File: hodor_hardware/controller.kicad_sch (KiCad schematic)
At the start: 42 parts, among them J4 USB_C_Receptacle_USB2.0_16P, J8 Conn_01x04_Pin, J9 Conn_01x04_Pin, SW1 SW_RST, SW2 SW_BOOT, T21 SCL, T24 SDA, U1 ESP32-S3-WROOM-1_N8R2, U6 MAX811SEUS-T, U9 24LC256

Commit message: Schematic finished
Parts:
- removed C20: 100p, Capacitor_SMD:C_0402_1005Metric, symbol Device:C
- removed R29: 47R, Resistor_SMD:R_0402_1005Metric, symbol Device:R
- C14, C39: value 100n -> 100nF
- J8, J9: footprint (none) -> Connector_PinHeader_2.54mm:PinHeader_1x04_P2.54mm_Vertical
- T21, T24: now left out of the parts list
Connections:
- net ADC_IN5 is gone; now on an unnamed net: U1.17 (IO9)
- net ADC_CH1: now reaches R31.1
- net ADC_CH2: now reaches R30.1
- net ADC_CH3: now reaches R32.1
- net ADC_CH4: now reaches R36.1
- net at R1.1: now also U1.22 (IO14)
- net OUT_CTRL_1: now reaches U1.10 (IO17)
- net OUT_CTRL_2: now reaches U1.11 (IO18)
- net DRV_~{SF}: now reaches U1.16 (IO46)
- net DRV_PWM1: now reaches U1.24 (IO47)
- net DRV_PWM2: now reaches U1.25 (IO48)
- net DRV_EN: now reaches U1.26 (IO45)
- net ENCODER_A: now reaches U1.28 (IO35)
- net ENCODER_B: now reaches U1.29 (IO36)
- net INPUT_1: now reaches U1.30 (IO37)
- net INPUT_2: now reaches U1.31 (IO38)
- net INPUT_3: now reaches U1.32 (IO39)
- net INPUT_4: now reaches U1.33 (IO40)
- net SAFETY_~{CLR}: now reaches U1.34 (IO41)
- net SAFETY_TRIG: now reaches U1.35 (IO42)
- net RELAY_CTRL_1: now reaches U1.8 (IO15)
- net RELAY_CTRL_2: now reaches U1.9 (IO16)
- no-connect marks 4 -> 5
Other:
- note added: "Status LEDs"
- moved on the sheet: D1, D2, R1, R2

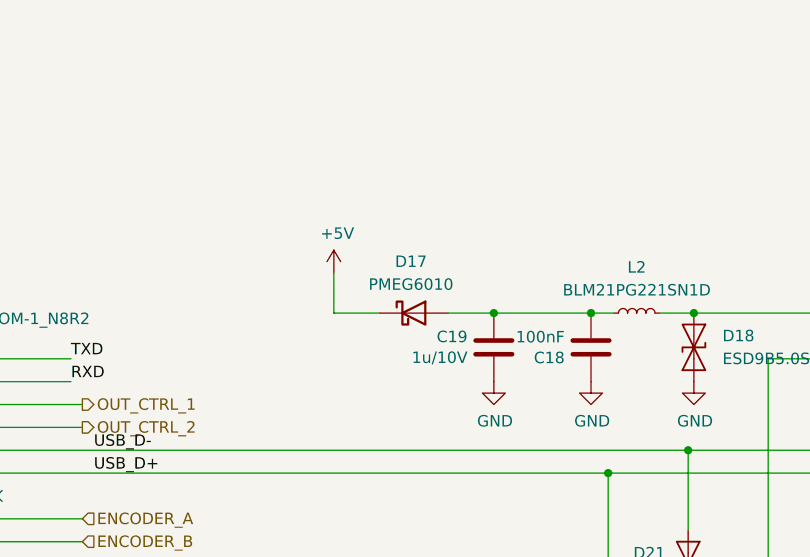
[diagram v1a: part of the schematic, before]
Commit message: Added USB switchover function for 5V
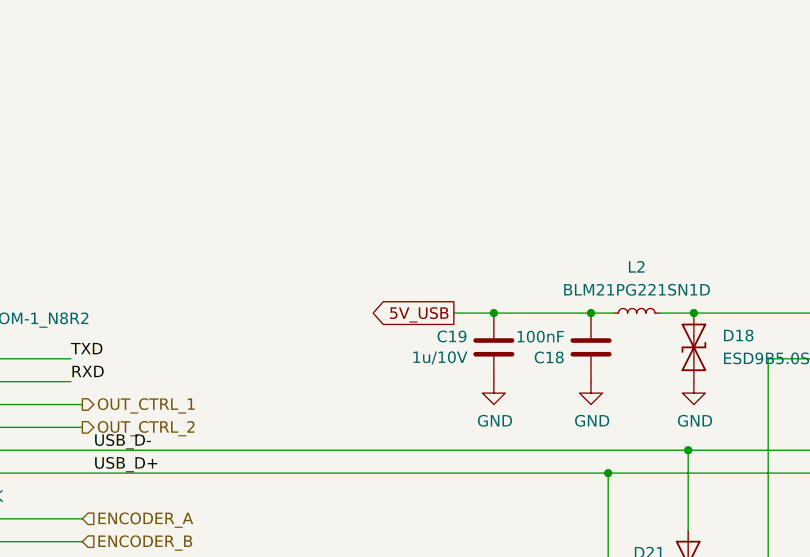
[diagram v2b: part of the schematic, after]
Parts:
- removed D17: PMEG6010, Diode_SMD:D_SOD-123F, symbol Device:D_Schottky
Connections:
- net 5V_USB: now reaches C18.1, C19.2, L2.1
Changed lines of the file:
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@@
 	(wire
 		(pts
-			(xy 171.45 45.72) (xy 166.37 45.72)
-		)
-		(stroke
-			(width 0)
-			(type default)
-		)
-	)
-	(wire
-		(pts
 			(xy 88.9 86.36) (xy 98.425 86.36)
 		)
@@
 		)
 	)
-	(wire
-		(pts
-			(xy 166.37 41.275) (xy 166.37 45.72)
-		)
-		(stroke
-			(width 0)
-			(type default)
-		)
-	)
 	(bus
 		(pts
@@
 	(wire
 		(pts
-			(xy 179.07 45.72) (xy 184.15 45.72)
+			(xy 179.705 45.72) (xy 184.15 45.72)
 		)
 		(stroke
@@
 		)
 	)
+	(global_label "5V_USB"
+		(shape output)
+		(at 179.705 45.72 180)
+		(fields_autoplaced yes)
+		(effects
+			(font
+				(size 1.27 1.27)
+			)
+			(justify right)
+		)
+		(property "Intersheetrefs" "${INTERSHEET_REFS}"
+			(at 169.6441 45.72 0)
+			(effects
+				(font
+					(size 1.27 1.27)
+				)
+				(justify right)
+			)
+		)
+	)
 	(hierarchical_label "RELAY_CTRL_1"
 		(shape output)
@@
 	)
 	(symbol
-		(lib_id "Device:D_Schottky")
-		(at 175.26 45.72 0)
-		(unit 1)
-		(exclude_from_sim no)
-		(in_bom yes)
-		(on_board yes)
-		(dnp no)
-		(fields_autoplaced yes)
-		(property "Reference" "D17"
-			(at 174.9425 40.005 0)
-			(effects
-				(font
-					(size 1.27 1.27)
-				)
-			)
-		)
-		(property "Value" "PMEG6010"
-			(at 174.9425 42.545 0)
-			(effects
-				(font
-					(size 1.27 1.27)
-				)
-			)
-		)
-		(property "Footprint" "Diode_SMD:D_SOD-123F"
-			(at 175.26 45.72 0)
-			(effects
-				(font
-					(size 1.27 1.27)
-				)
-				(hide yes)
-			)
-		)
-		(property "Datasheet" "~"
-			(at 175.26 45.72 0)
-			(effects
-				(font
-					(size 1.27 1.27)
-				)
-				(hide yes)
-			)
-		)
-		(property "Description" "Schottky diode"
-			(at 175.26 45.72 0)
-			(effects
-				(font
-					(size 1.27 1.27)
-				)
-				(hide yes)
-			)
-		)
-		(pin "2"
-		)
-		(pin "1"
-		)
-		(instances
-			(project "hodor_hardware"
-				(path "/2da01e60-41ef-423d-82f4-a5c8908d8b96/efd4ec69-52b7-4b82-b6f7-297e43729fd0"
-					(reference "D17")
-					(unit 1)
-				)
-			)
-		)
-	)
-	(symbol
 		(lib_id "Hodor-rescue:GND-power")
 		(at 46.355 130.81 0)
@@
 					(unit 1)
 				)
-			)
-		)
-	)
-	(symbol
-		(lib_id "Hodor-rescue:+5V-power")
-		(at 166.37 41.275 0)
-		(unit 1)
-		(exclude_from_sim no)
-		(in_bom yes)
-		(on_board yes)
-		(dnp no)
-		(property "Reference" "#PWR060"
-			(at 166.37 45.085 0)
-			(effects
-				(font
-					(size 1.27 1.27)
-				)
-				(hide yes)
-			)
-		)
-		(property "Value" "+5V"
-			(at 166.751 36.8808 0)
-			(effects
-				(font
-					(size 1.27 1.27)
-				)
-			)
-		)
-		(property "Footprint" ""
-			(at 166.37 41.275 0)
-			(effects
-				(font
-					(size 1.27 1.27)
-				)
-				(hide yes)
-			)
-		)
-		(property "Datasheet" ""
-			(at 166.37 41.275 0)
-			(effects
-				(font
-					(size 1.27 1.27)
-				)
-				(hide yes)
-			)
-		)
-		(property "Description" ""
-			(at 166.37 41.275 0)
-			(effects
-				(font
-					(size 1.27 1.27)
-				)
-				(hide yes)
-			)
-		)
-		(pin "1"
-		)
-		(instances
-			(project "hodor_hardware"
-				(path "/2da01e60-41ef-423d-82f4-a5c8908d8b96/efd4ec69-52b7-4b82-b6f7-297e43729fd0"
-					(reference "#PWR060")
-					(unit 1)
-				)

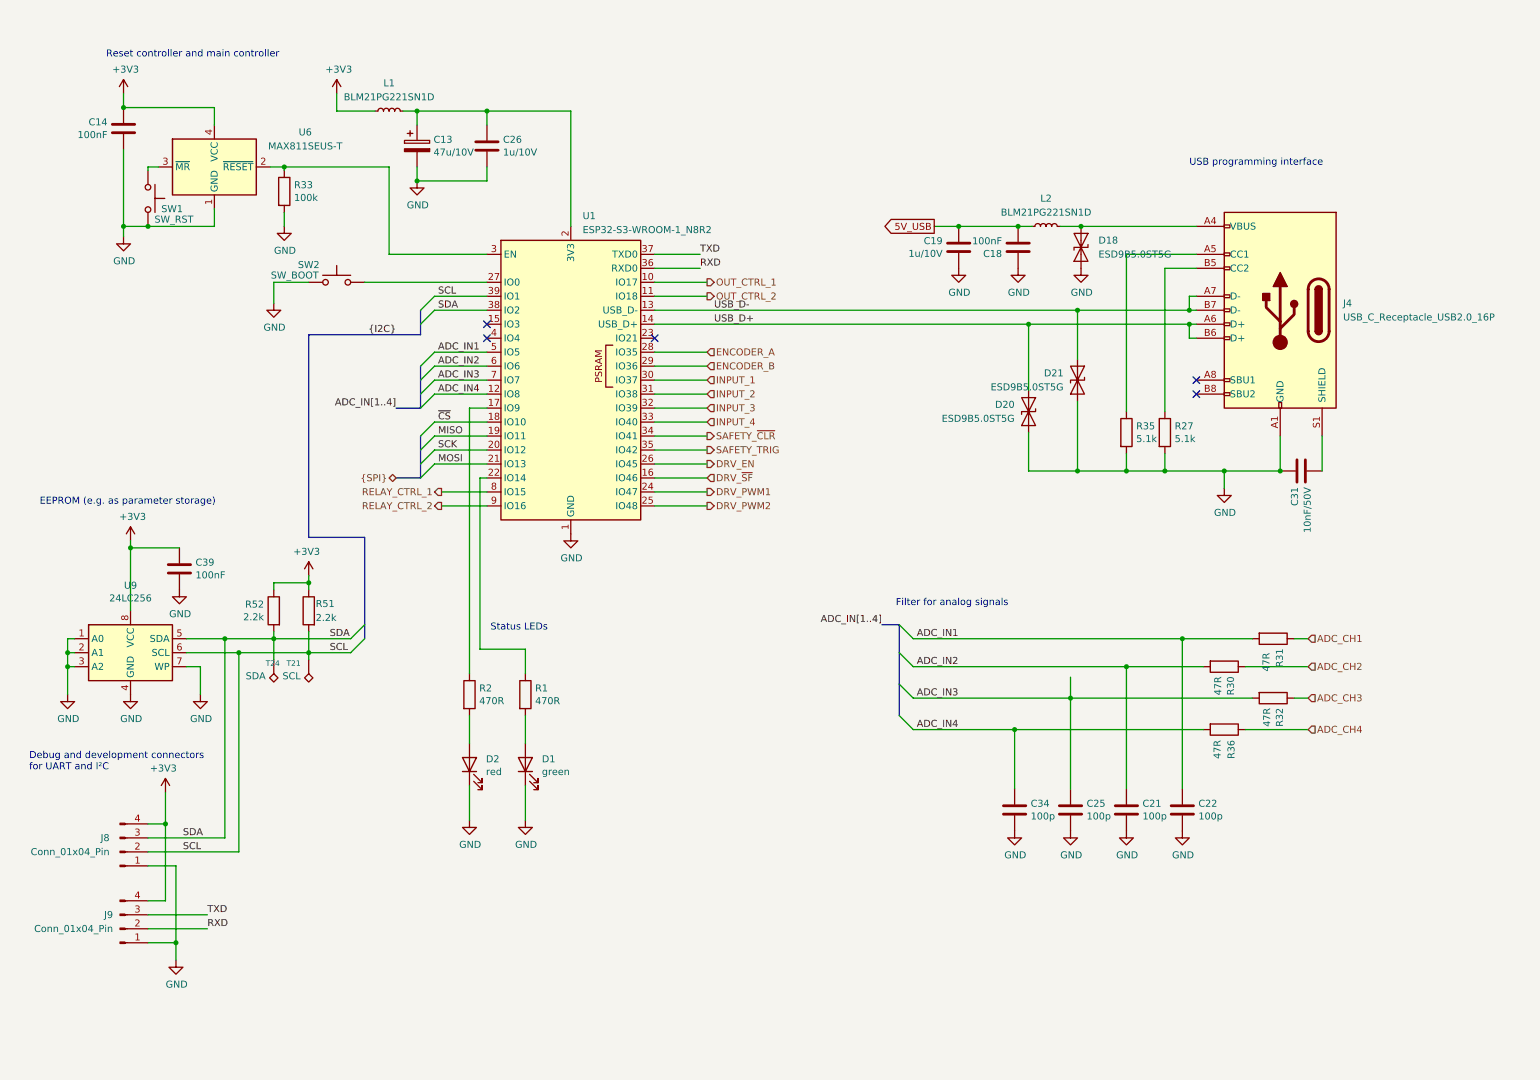
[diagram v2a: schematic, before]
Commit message: Reworked into 2 PCBs
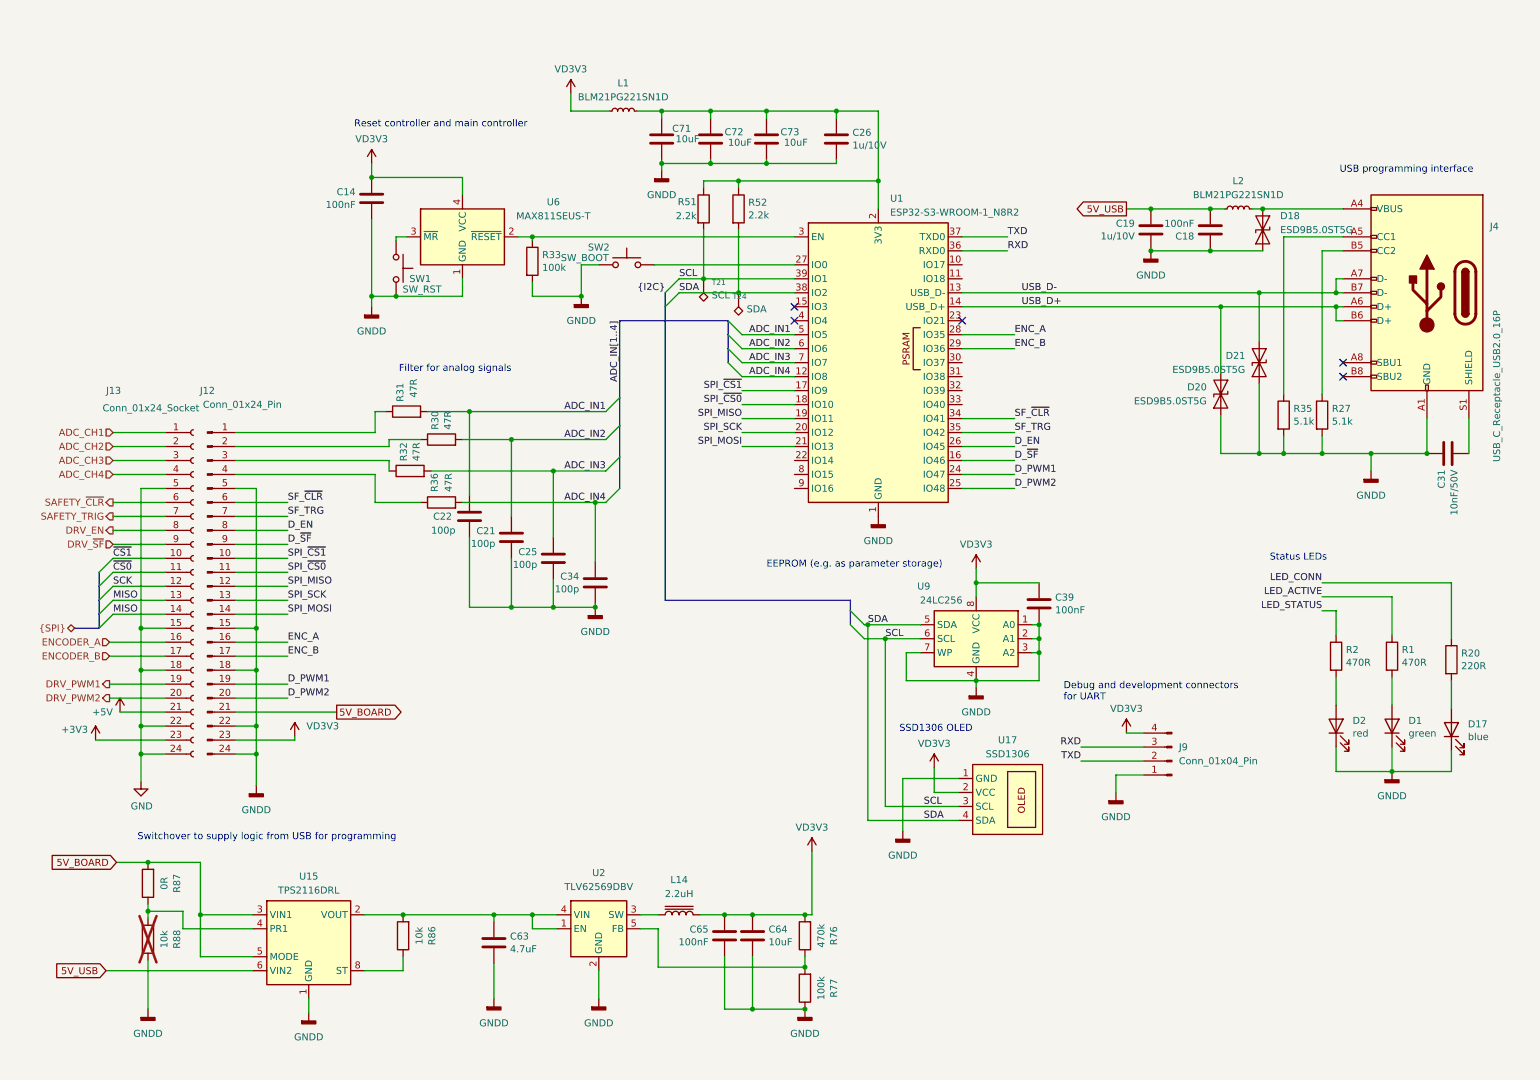
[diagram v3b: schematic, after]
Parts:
- removed C13: 47u/10V, Capacitor_SMD:C_Elec_5x5.4, symbol Hodor-rescue:C_Polarized-Device
- removed J8: Conn_01x04_Pin, Connector_PinHeader_2.54mm:PinHeader_1x04_P2.54mm_Vertical, symbol Connector:Conn_01x04_Pin
- added C63: 4.7uF, Capacitor_SMD:C_1206_3216Metric, symbol Device:C
- added C64, C71, C72, C73: 10uF, Capacitor_SMD:C_0805_2012Metric, symbol Device:C
- added C65: 100nF, Capacitor_SMD:C_0402_1005Metric, symbol Device:C
- added D17: blue, LED_SMD:LED_Kingbright_APA1606_1.6x0.6mm_Horizontal, symbol Device:LED
- added J12: Conn_01x24_Pin, Connector_PinHeader_2.00mm:PinHeader_2x12_P2.00mm_Horizontal, symbol Connector:Conn_01x24_Pin
- added J13: Conn_01x24_Socket, Connector_PinSocket_2.00mm:PinSocket_2x12_P2.00mm_Vertical, symbol Connector:Conn_01x24_Socket
- added L14: 2.2uH, Inductor_SMD:L_1812_4532Metric, symbol Device:L_Iron
- added R20: 220R, Resistor_SMD:R_0402_1005Metric, symbol Device:R
- added R76: 470k, Resistor_SMD:R_0402_1005Metric, symbol Device:R
- added R77: 100k, Resistor_SMD:R_0402_1005Metric, symbol Device:R
- added R86, R88: 10k, Resistor_SMD:R_0402_1005Metric, symbol Device:R
- added R87: 0R, Resistor_SMD:R_0402_1005Metric, symbol Device:R
- added U15: TPS2116DRL, Package_TO_SOT_SMD:SOT-583-8, symbol Power_Management:TPS2116DRL
- added U17: SSD1306, hodor_footprints:SSD1306_OLED_Horizontal_Reverse, symbol hodor_custom_parts:SSD1306_OLED
- added U2: TLV62569DBV, Package_TO_SOT_SMD:SOT-23-5, symbol Regulator_Switching:TLV62569DBV
- D1, D2: footprint LED_SMD:LED_0603_1608Metric -> LED_SMD:LED_Kingbright_APA1606_1.6x0.6mm_Horizontal
- J9: footprint Connector_PinHeader_2.54mm:PinHeader_1x04_P2.54mm_Vertical -> hodor_footprints:Conn_Header2.54_1x04_SMD
- SW1, SW2: footprint Button_Switch_SMD:SW_Push_SPST_NO_Alps_SKRK -> Button_Switch_SMD:SW_SPST_CK_KMS2xxG
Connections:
- net +3V3: now also J13.23 (Pin_23); no longer C14.2, C39.2, J9.4 (Pin_4), L1.1, R51.1, R52.1, U6.4 (VCC), U9.8 (VCC)
- net 5V_USB: now also U15.6 (VIN2)
- net ADC_CH1: now also J13.1 (Pin_1); no longer R31.1
- net ADC_CH2: now also J13.2 (Pin_2); no longer R30.1
- net ADC_CH3: now also J13.3 (Pin_3); no longer R32.1
- net ADC_CH4: now also J13.4 (Pin_4); no longer R36.1
- net DRV_EN: now also J13.8 (Pin_8); no longer U1.26 (IO45)
- net DRV_PWM1: now also J13.19 (Pin_19); no longer U1.24 (IO47)
- net DRV_PWM2: now also J13.20 (Pin_20); no longer U1.25 (IO48)
- net DRV_~{SF}: now also J13.9 (Pin_9); no longer U1.16 (IO46)
- net ENCODER_A: now also J13.16 (Pin_16); no longer U1.28 (IO35)
- net ENCODER_B: now also J13.17 (Pin_17); no longer U1.29 (IO36)
- net GND: now also J13.15 (Pin_15), J13.18 (Pin_18), J13.22 (Pin_22), J13.24 (Pin_24), J13.5 (Pin_5); no longer C14.1, C18.2, C19.1, C21.1, C22.1, C25.1, C26.1, C31.2, C34.1, C39.1, D1.1 (K), D18.1 (A1), D2.1 (K), D20.1 (A1), D21.1 (A1), J4.A1 (GND), J4.A12 (GND), J4.B1 (GND), J4.B12 (GND), J9.1 (Pin_1), R27.2, R33.2, R35.2, SW1.1, SW2.1, U1.1 (GND), U1.40 (GND), U1.41 (GND), U6.1 (GND), U9.1 (A0), U9.2 (A1), U9.3 (A2), U9.4 (GND), U9.7 (WP)
- net MISO: now also J13.13 (Pin_13), J13.14 (Pin_14); no longer U1.19 (IO11)
- net RXD: now also J9.3 (Pin_3); no longer J9.2 (Pin_2)
- net SAFETY_TRIG: now also J13.7 (Pin_7); no longer U1.35 (IO42)
- net SAFETY_~{CLR}: now also J13.6 (Pin_6); no longer U1.34 (IO41)
- net SCK: now also J13.12 (Pin_12); no longer U1.20 (IO12)
- net SCL: now also U17.3 (SCL)
- net SDA: now also U17.4 (SDA)
- net TXD: now also J9.2 (Pin_2); no longer J9.3 (Pin_3)
- net at C26.2, L1.2, U1.2 (3V3): now also R51.1, R52.1, C71.1, C72.1, C73.1
- net LED_STATUS: now reaches R2.1
- net LED_STATUS: no longer U1.17 (IO9)
- net at U1.22 (IO14): no longer R1.1
- net INPUT_1: no longer names the net of U1.30 (IO37)
- net INPUT_2: no longer names the net of U1.31 (IO38)
- net INPUT_3: no longer names the net of U1.32 (IO39)
- net INPUT_4: no longer names the net of U1.33 (IO40)
- net MOSI renamed SPI_MOSI
- net SPI_MOSI: now also J12.14 (Pin_14)
- net OUT_CTRL_1: no longer names the net of U1.10 (IO17)
- net OUT_CTRL_2: no longer names the net of U1.11 (IO18)
- net RELAY_CTRL_1: no longer names the net of U1.8 (IO15)
- net RELAY_CTRL_2: no longer names the net of U1.9 (IO16)
- net ~{CS} renamed SPI_~{CS0}
- net SPI_~{CS0}: now also J12.11 (Pin_11)
- new net: J12.1 (Pin_1), R31.1
- new net: J12.2 (Pin_2), R30.1
- new net: J12.3 (Pin_3), R32.1
- new net: J12.4 (Pin_4), R36.1
- new net: R86.1, U15.8 (ST)
- new net: C63.1, R86.2, U15.2 (VOUT), U15.7 (VOUT), U2.1 (EN), U2.4 (VIN)
- new net: D17.2 (A), R20.2
- new net: L14.1, U2.3 (SW)
- new net: R76.1, R77.2, U2.5 (FB)
- new net: R87.1, R88.2, U15.4 (PR1)
- new net +5V: J13.21 (Pin_21)
- new net 5V_BOARD: J12.21 (Pin_21), R87.2, U15.3 (VIN1), U15.5 (MODE)
- new net D_EN: J12.8 (Pin_8), U1.26 (IO45)
- new net D_PWM1: J12.19 (Pin_19), U1.24 (IO47)
- new net D_PWM2: J12.20 (Pin_20), U1.25 (IO48)
- new net D_~{SF}: J12.9 (Pin_9), U1.16 (IO46)
- new net ENC_A: J12.16 (Pin_16), U1.28 (IO35)
- new net ENC_B: J12.17 (Pin_17), U1.29 (IO36)
- new net GNDD: C14.1, C18.2, C19.1, C21.1, C22.1, C25.1, C26.1, C31.2, C34.1, C39.1, C63.2, C64.2, C65.2, C71.2, C72.2, C73.2, D1.1 (K), D17.1 (K), D18.1 (A1), D2.1 (K), D20.1 (A1), D21.1 (A1), J12.15 (Pin_15), J12.18 (Pin_18), J12.22 (Pin_22), J12.24 (Pin_24), J12.5 (Pin_5), J4.A1 (GND), J4.A12 (GND), J4.B1 (GND), J4.B12 (GND), J9.1 (Pin_1), R27.2, R33.2, R35.2, R77.1, R88.1, SW1.1, SW2.1, U1.1 (GND), U1.40 (GND), U1.41 (GND), U15.1 (GND), U17.1 (GND), U2.2 (GND), U6.1 (GND), U9.1 (A0), U9.2 (A1), U9.3 (A2), U9.4 (GND), U9.7 (WP)
- new net LED_ACTIVE: R1.1
- new net LED_CONN: R20.1
- new net SF_TRG: J12.7 (Pin_7), U1.35 (IO42)
- new net SF_~{CLR}: J12.6 (Pin_6), U1.34 (IO41)
- new net SPI_MISO: J12.12 (Pin_12), U1.19 (IO11)
- new net SPI_SCK: J12.13 (Pin_13), U1.20 (IO12)
- new net SPI_~{CS1}: J12.10 (Pin_10), U1.17 (IO9)
- new net VD3V3: C14.2, C39.2, C64.1, C65.1, J12.23 (Pin_23), J9.4 (Pin_4), L1.1, L14.2, R76.2, U17.2 (VCC), U6.4 (VCC), U9.8 (VCC)
- new net ~{CS0}: J13.11 (Pin_11)
- new net ~{CS1}: J13.10 (Pin_10)
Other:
- note added: "Debug and development connectors for UART"
- note added: "SSD1306 OLED"
- note added: "Switchover to supply logic from USB for programming"
- note removed: "Debug and development connectors for UART and I²C"
- moved on the sheet: C14, C18, C19, C21, C22, C25, C26, C31, C34, C39, D1, D18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
